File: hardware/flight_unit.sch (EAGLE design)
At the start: 7 parts, among them IC2 7805T, J1 DCJ0202

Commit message: created master schematic
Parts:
- removed R_LOAD: (no value), rcl:R-US_0207/10
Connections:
- removed net N$3: IC2.VO, R_LOAD.1
- new net +3V3: IC2.VO
- net 0: no longer R_LOAD.2
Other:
- note added: "POWER"
- note added: "University of Pittsburgh ECE Senior Design Fall 2020 Team 5 (Stumpp, Corcoran)"
- note removed: "V_IN"

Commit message: finished teplate and added pynq-z2 connector
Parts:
- added J2: CONN_20X2SHROUDED, SparkFun-Connectors:CONN_20X2SHROUDED
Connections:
- removed net 0: BATTERY.-, IC2.GND, J1.2
- new net GND: BATTERY.-, IC2.GND, J1.2, J2.14, J2.20, J2.25, J2.30, J2.34, J2.39, J2.6, J2.9
- new net SC_3V3: J2.1, J2.17
- new net SC_5V0: J2.2, J2.4
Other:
- note added: "01 02 03 04 05 06"
- note added: "Content"
- note added: "Cover Page Power Regulation and Supply Pynq-z2 I/O Bank MCU Memory Sensors and Discretes"
- note added: "MCU"
- note added: "Memory"
- note added: "Power Regulation and Supply"
- note added: "Pynq-z2 I/O Bank"
- note added: "Real Time Monitor For Space Missions Flight Unit Hardware"
- note added: "Sensors and Discretes"
- note added: "Sheet"
- note removed: "POWER"

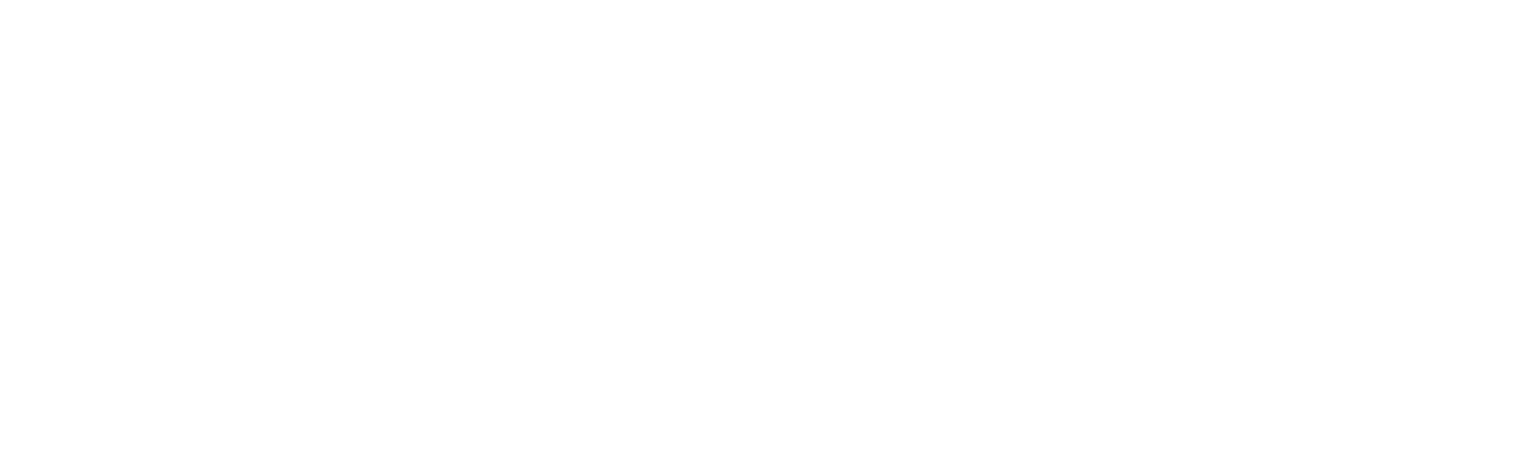
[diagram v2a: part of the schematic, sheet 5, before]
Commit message: added fram and MCU
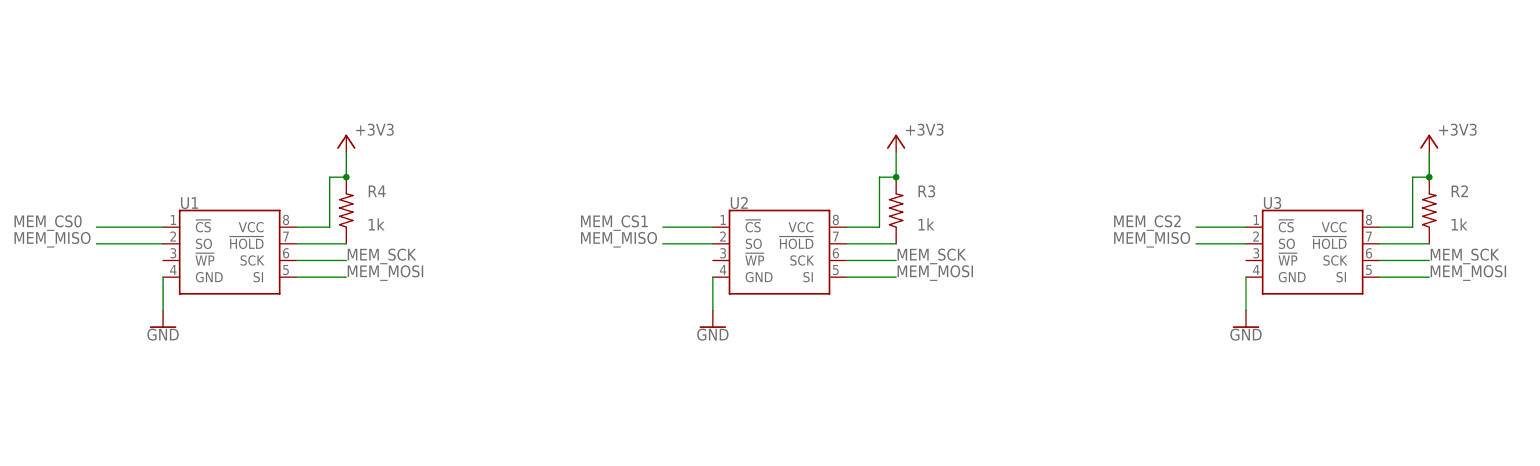
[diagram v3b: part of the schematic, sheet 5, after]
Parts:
- added R2, R3, R4: 1k, resistor:R-US_R1210
- added U$1: TEENSY_4.0, TEENSY 4.0:TEENSY_4.0
- added U1, U2, U3: 4MB Flash, SparkFun-IC-Memory:AT25SF041
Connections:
- new net A_0: U$1.20/A6/TX5
- new net A_1: U$1.21/A7/RX5
- new net A_2: U$1.22/A8
- new net A_3: U$1.23/A9
- new net D_0: U$1.0/RX1
- new net D_1: U$1.1/TX1
- new net D_2: U$1.2
- new net D_3: U$1.3
- new net D_4: U$1.4
- new net IIC_SCL: U$1.19/A5/SCL
- new net IIC_SDA: U$1.18/A4/SDA
- new net LED_0: U$1.5
- new net LED_1: U$1.6
- new net LED_2: U$1.7/RX2
- new net MEM_CS0: U$1.10/CS, U1.!CS
- new net MEM_CS1: U$1.9, U2.!CS
- new net MEM_CS2: U$1.8/TX2, U3.!CS
- new net MEM_MISO: U$1.12/MISO, U1.SO, U2.SO, U3.SO
- new net MEM_MOSI: U$1.11/MOSI, U1.SI, U2.SI, U3.SI
- new net MEM_SCK: U$1.13/SCK, U1.SCK, U2.SCK, U3.SCK
- new net N$3: R2.1, U3.!HOLD
- new net N$5: R4.1, U1.!HOLD
- new net N$6: R3.1, U2.!HOLD
- new net NC: U$1.3V3_LO
- new net T_0: U$1.14/A0/TX3
- new net T_1: U$1.15/A1/RX3
- new net V_0: U$1.16/A2/RX4
- new net V_1: U$1.17/A3/TX4
- net +3V3: now also R2.2, R3.2, R4.2, U$1.VIN, U1.VCC, U2.VCC, U3.VCC
- net GND: now also U$1.GND, U$1.GND2, U1.GND, U2.GND, U3.GND

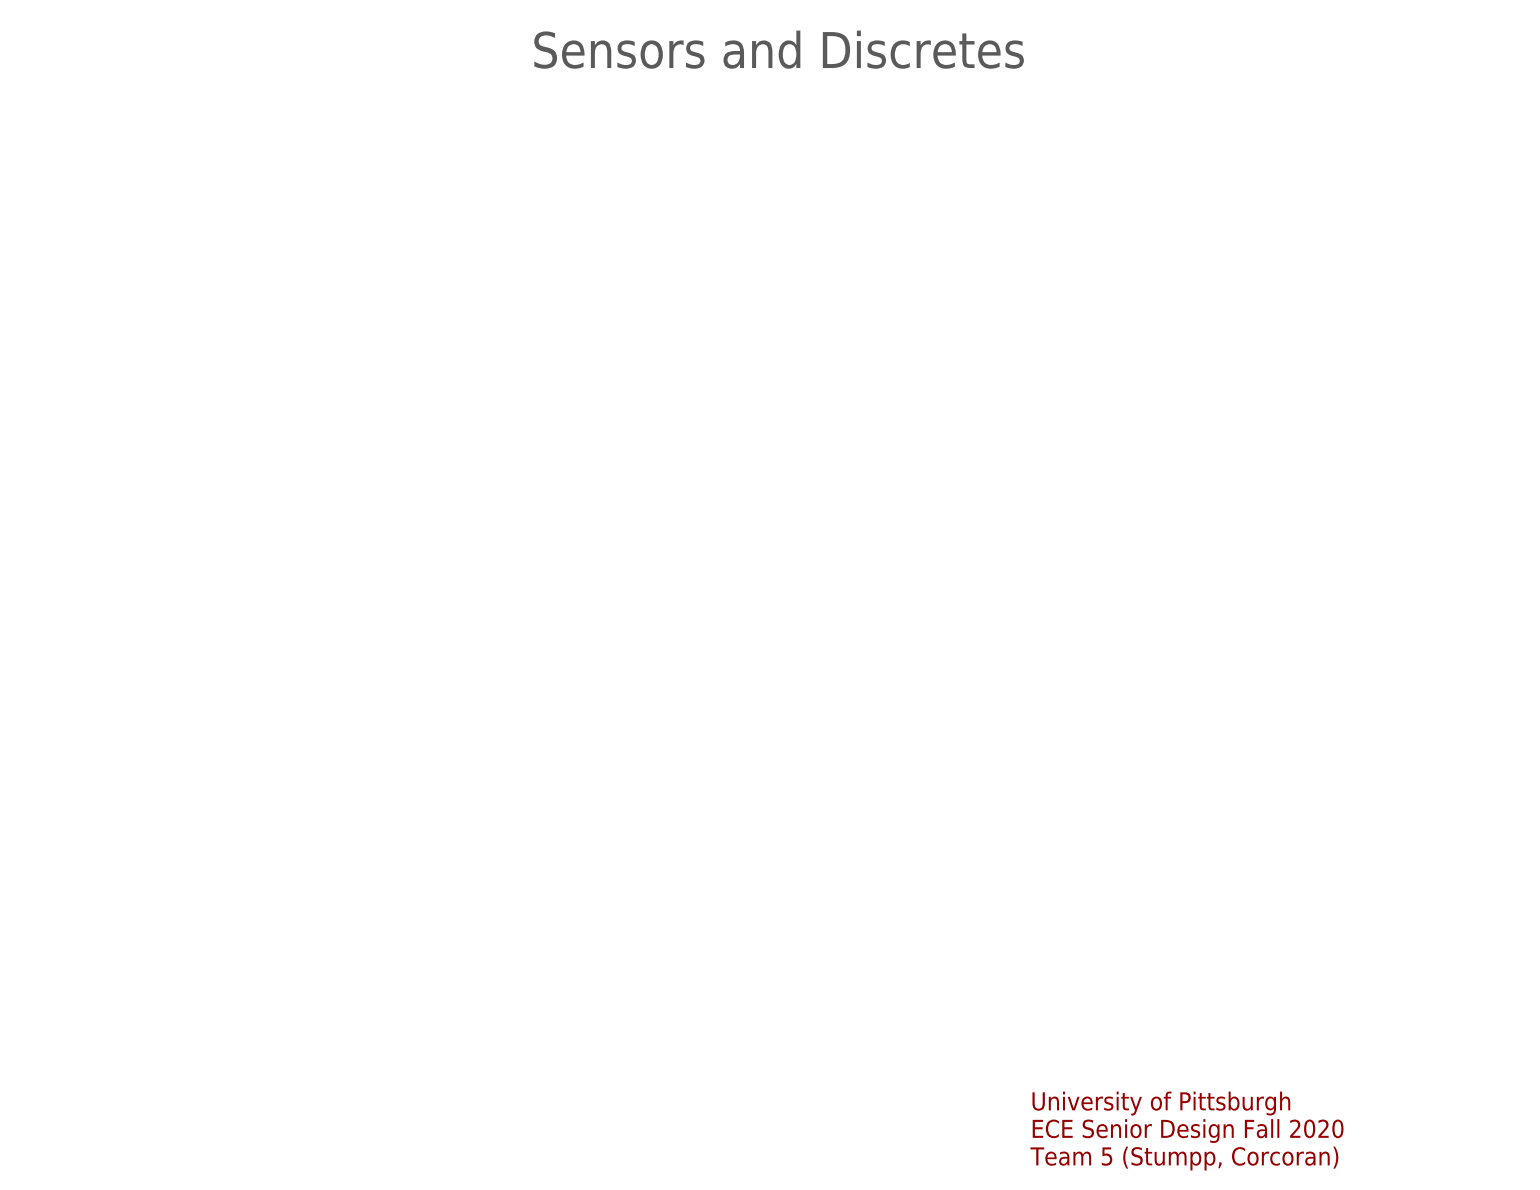
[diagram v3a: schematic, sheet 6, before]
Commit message: Added DIP resistor packages for analog bank
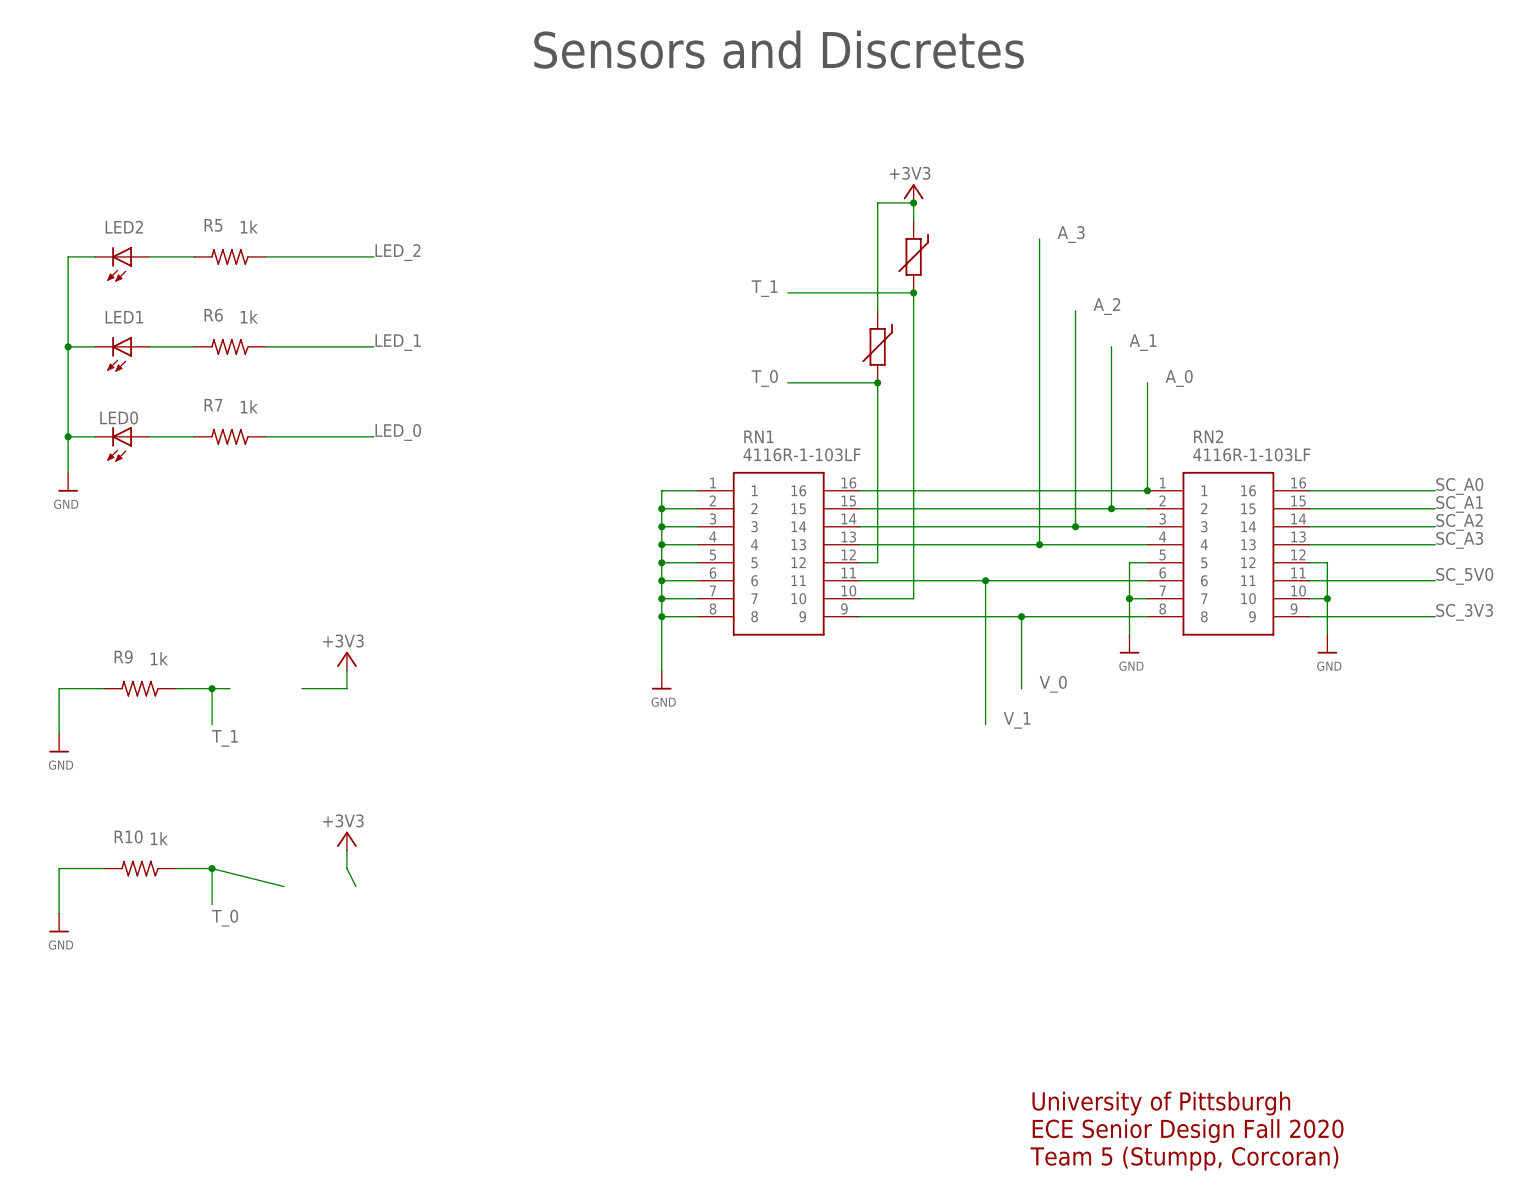
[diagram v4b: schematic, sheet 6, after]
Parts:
- added LED0, LED1, LED2: (no value), adafruit:LED3MM
- added R10, R5, R6, R7, R9: 1k, resistor:R-US_R1210
- added R8, T1: THERMISTOR-2,5, varistor:THERMISTOR-2,5
- added RN1, RN2: 4116R-1-103LF, SamacSys_Parts:4116R-1-103LF
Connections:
- new net N$13: LED2.A, R5.2
- new net N$7: LED0.A, R7.2
- new net N$8: LED1.A, R6.2
- new net SC_A0: RN2.16
- new net SC_A1: RN2.15
- new net SC_A2: RN2.14
- new net SC_A3: RN2.13
- net +3V3: now also R8.1, T1.1
- net A_0: now also RN1.16, RN2.1
- net A_1: now also RN1.15, RN2.2
- net A_2: now also RN1.14, RN2.3
- net A_3: now also RN1.13, RN2.4
- net GND: now also LED0.C, LED1.C, LED2.C, R10.2, R9.2, RN1.1, RN1.2, RN1.3, RN1.4, RN1.5, RN1.6, RN1.7, RN1.8, RN2.10, RN2.12, RN2.5, RN2.7
- net LED_0: now also R7.1
- net LED_1: now also R6.1
- net LED_2: now also R5.1
- net SC_3V3: now also RN2.9
- net SC_5V0: now also RN2.11
- net T_0: now also R10.1, R8.2, RN1.12
- net T_1: now also R9.1, RN1.10, T1.2
- net V_0: now also RN1.9, RN2.8
- net V_1: now also RN1.11, RN2.6

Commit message: Created and added IMU library part
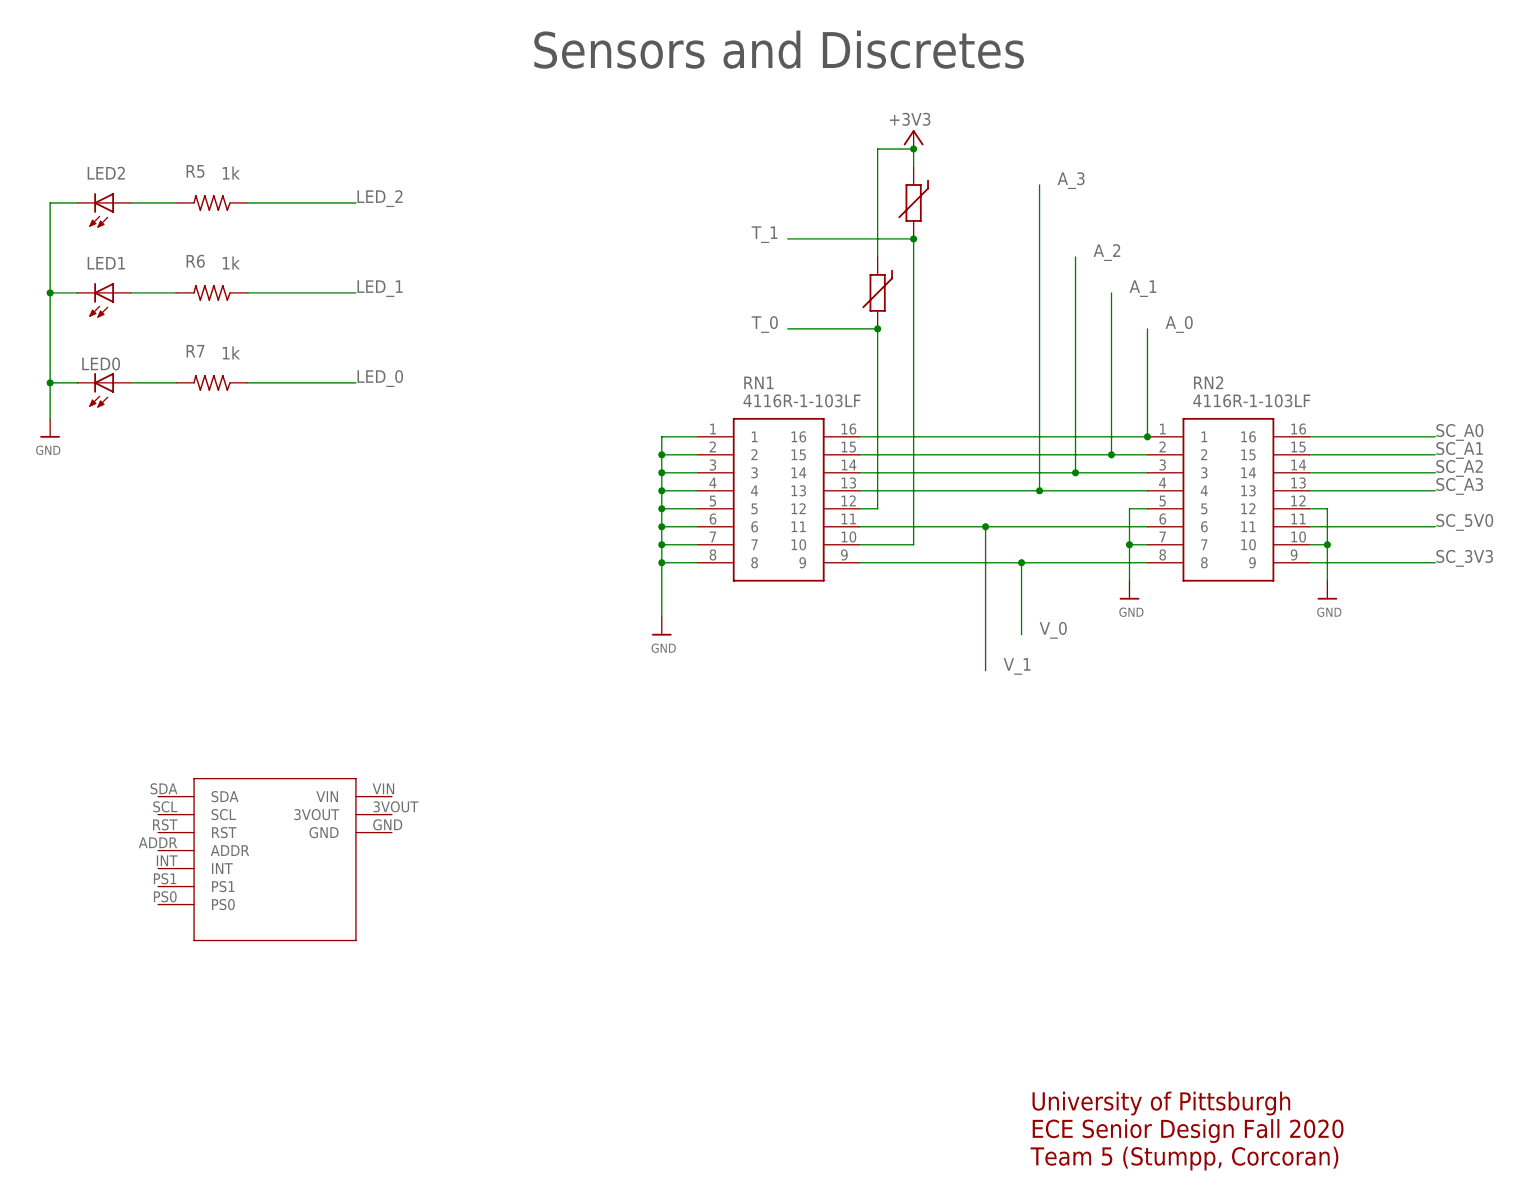
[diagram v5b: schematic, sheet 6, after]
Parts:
- removed R10, R9: 1k, resistor:R-US_R1210
- added U$3: IMU_BREAKOUT, adafruit:IMU_BREAKOUT
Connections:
- net GND: no longer R10.2, R9.2
- net T_0: no longer R10.1
- net T_1: no longer R9.1
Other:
- moved on the sheet: LED0, LED1, LED2, R5, R6, R7, RN1, RN2

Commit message: updated i/o headers
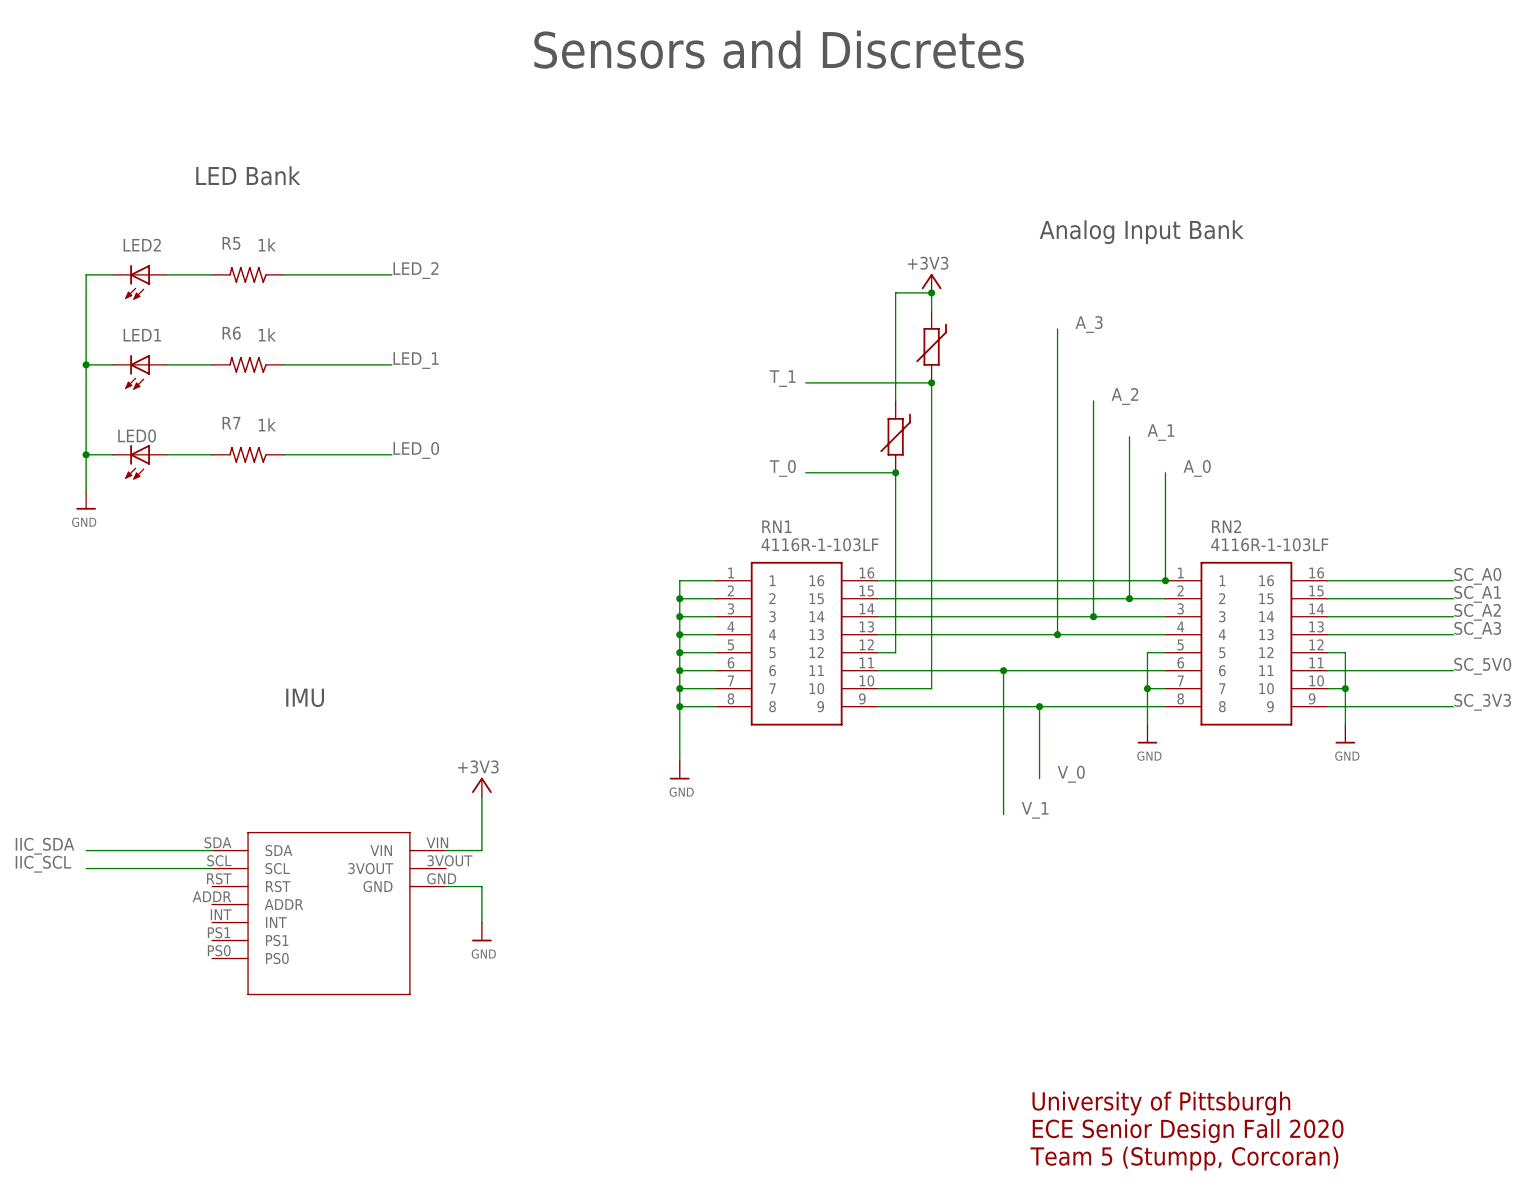
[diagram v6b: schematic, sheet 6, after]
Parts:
- added JP1: (no value), adafruit:PINHD-1X6B
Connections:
- removed net D_0: U$1.0/RX1
- removed net D_1: U$1.1/TX1
- removed net D_2: U$1.2
- removed net D_3: U$1.3
- removed net D_4: U$1.4
- new net SC_D0: J2.8, U$1.0/RX1
- new net SC_D1: J2.12, U$1.1/TX1
- new net SC_D2: J2.16, U$1.2
- new net SC_D3: J2.22, U$1.3
- new net SC_D4: J2.36, U$1.4
- net +3V3: now also U$3.VIN
- net GND: now also JP1.5, JP1.6, U$3.GND
- net IIC_SCL: now also J2.29, U$3.SCL
- net IIC_SDA: now also J2.7, U$3.SDA
- net SC_A0: now also JP1.1
- net SC_A1: now also JP1.2
- net SC_A2: now also JP1.3
- net SC_A3: now also JP1.4
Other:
- note added: "Analog Input Bank"
- note added: "Analog Test"
- note added: "Cover Page Power Regulation and Supply I/O Headers MCU Memory Sensors and Discretes"
- note added: "FRAM 0"
- note added: "FRAM 1"
- note added: "FRAM 2"
- note added: "I/O Headers"
- note added: "IMU"
- note added: "LED Bank"
- note added: "Pynq-z2 RPI"
- note removed: "Cover Page Power Regulation and Supply Pynq-z2 I/O Bank MCU Memory Sensors and Discretes"
- note removed: "Pynq-z2 I/O Bank"
- moved on the sheet: J2, LED0, LED1, LED2, R2, R3, R4, R5, R6, R7, RN1, RN2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
